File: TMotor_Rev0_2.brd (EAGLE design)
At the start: 91.5 x 74.3 mm, 78 parts, among them J1 5015680507, J10 5015680207, J2 5015680507, J7 5015680207, J8 5015680207, J9 5015680207, U1 INA125U, U2 INA125U, U3 INA125U, U4 INA125U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

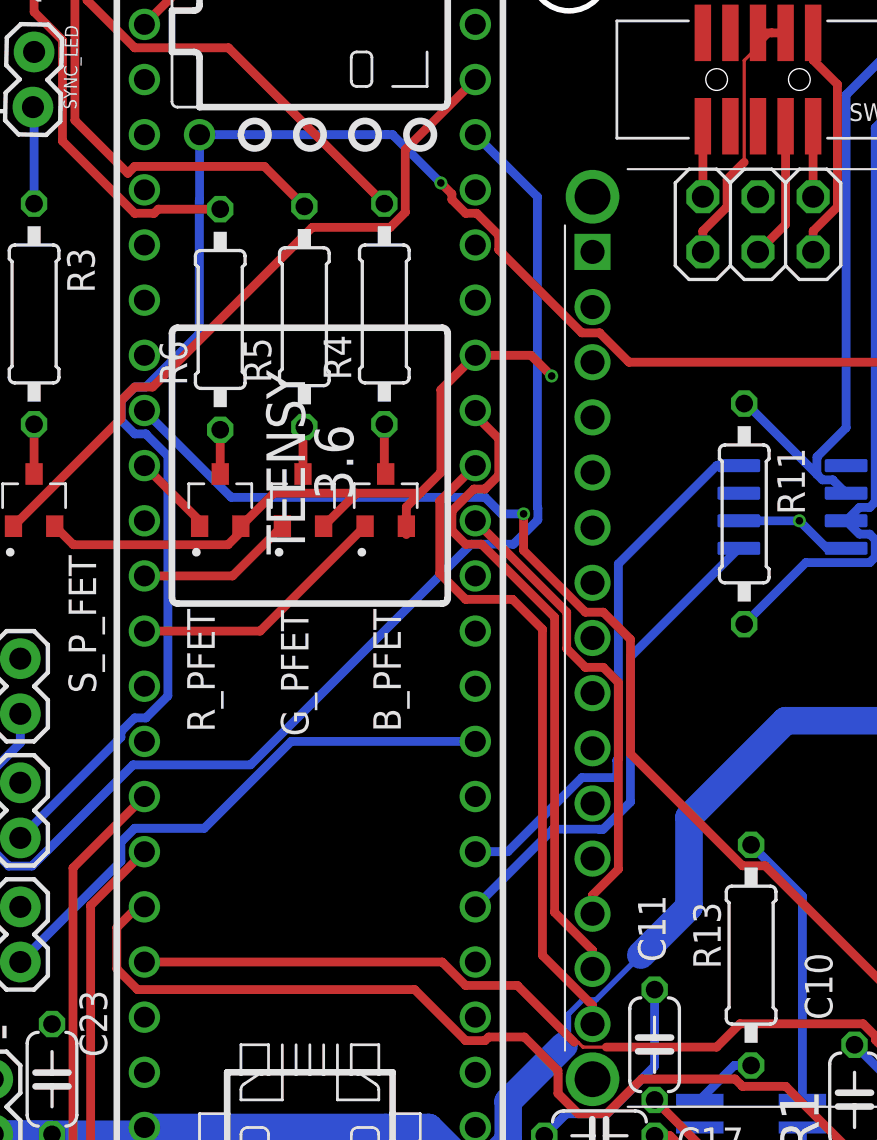
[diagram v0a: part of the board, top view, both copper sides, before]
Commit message: created CIPO COPI transfer spot
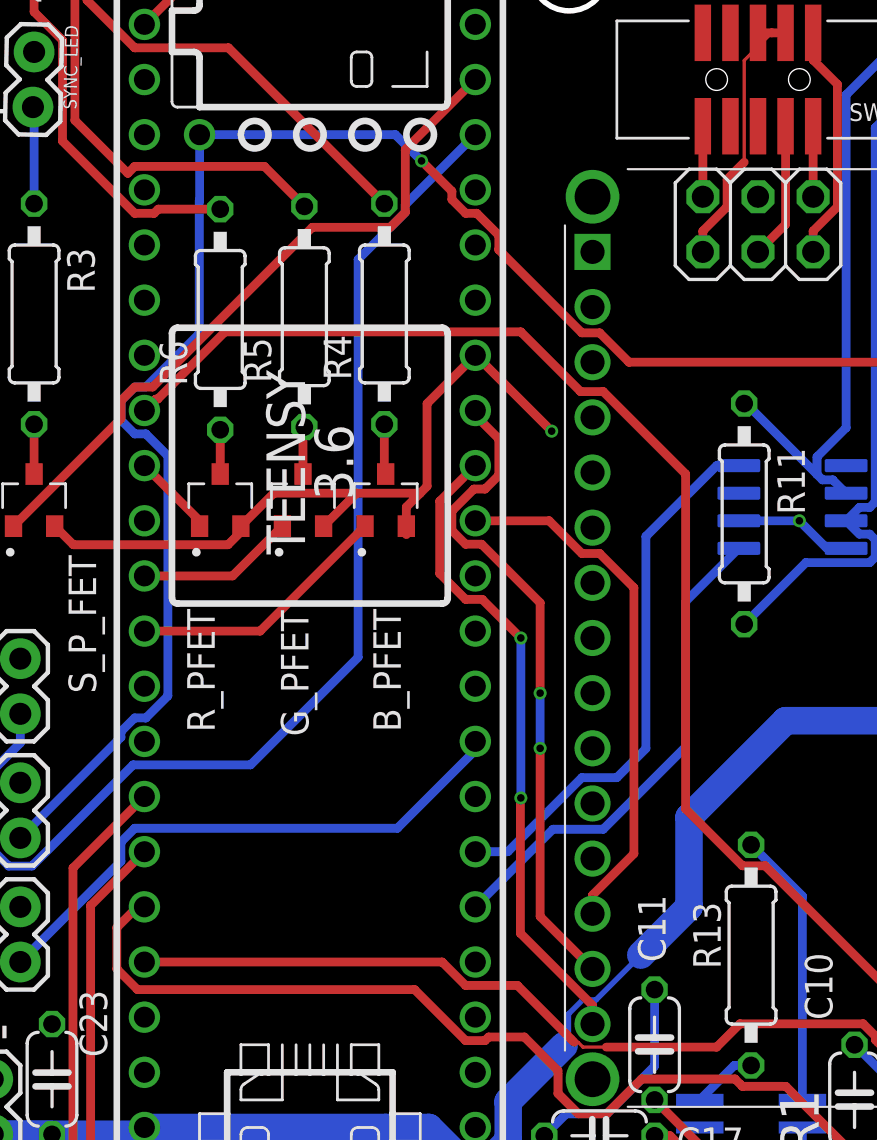
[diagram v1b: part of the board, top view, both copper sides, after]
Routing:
- net SCK: track 51.7 -> 59.6 mm, vias 1 -> 0
- net SYNC_DEFAULT: track 57.8 -> 54.2 mm
- net NANO_CS: track 21.8 -> 24.4 mm
- net 3.3V: track 62.1 -> 63.1 mm
- net MISO: track 30.6 -> 29.8 mm, vias 0 -> 2
- net MOSI: vias 0 -> 2

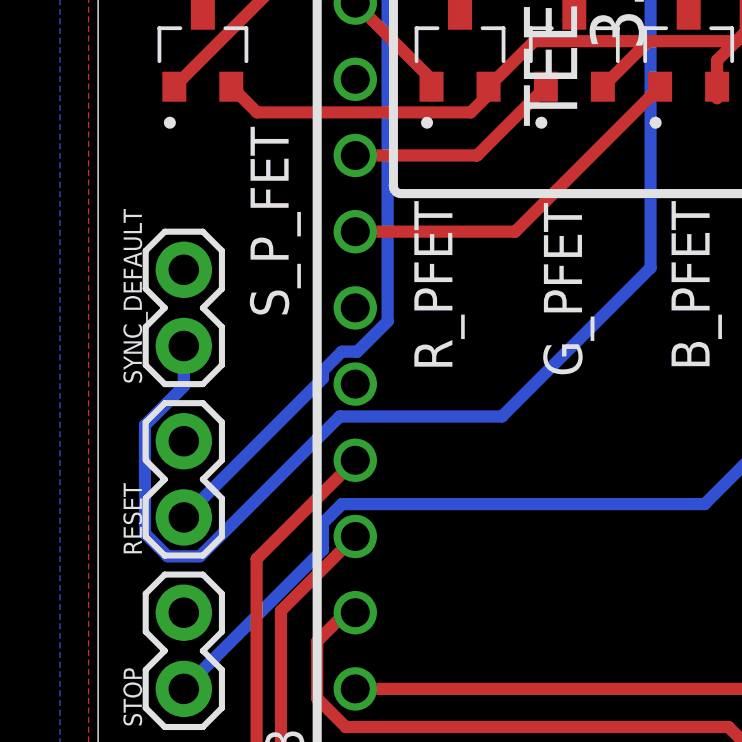
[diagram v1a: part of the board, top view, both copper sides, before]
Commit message: repositioned headers for switches
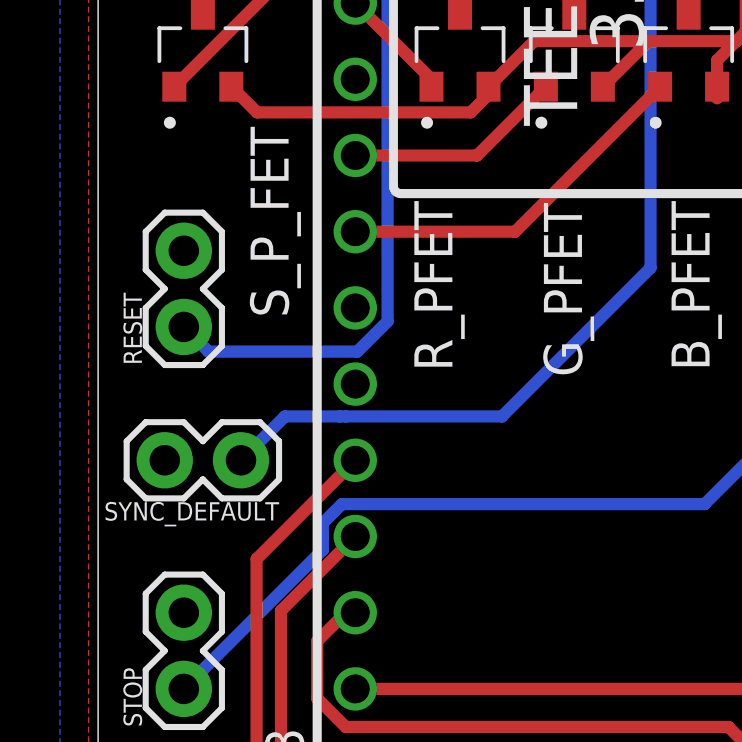
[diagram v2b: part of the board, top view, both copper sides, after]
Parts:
- moved RESET 6.35 mm to (-30.8, 35.9)
- moved SYNC_DEFAULT 4.26 mm to (-28.9, 31.4), turned to 180 degrees
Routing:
- net SYNC_DEFAULT: track 54.2 -> 42.6 mm
- net RESET: track 76.8 -> 74.7 mm
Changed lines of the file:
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@@
 </element>
 <element name="U$1" library="Teensy356" package="TEENSY_3.5/3.6_EXTERNAL_W/RESET" value="TEENSY_3.5/3.6_EXTERNAL_W/RESET" x="-17.4625" y="44.1325" smashed="yes" rot="R90"/>
-<element name="RESET" library="SparkFun-Connectors" library_urn="urn:adsk.eagle:library:513" package="1X02" package3d_urn="urn:adsk.eagle:package:38039/1" value="" x="-30.7975" y="29.5275" smashed="yes" rot="R90">
-<attribute name="NAME" x="-32.1945" y="28.2575" size="0.6096" layer="25" font="vector" ratio="20" rot="R90"/>
-<attribute name="VALUE" x="-28.7655" y="28.2575" size="0.6096" layer="27" font="vector" ratio="20" rot="R90"/>
-</element>
-<element name="SYNC_DEFAULT" library="SparkFun-Connectors" library_urn="urn:adsk.eagle:library:513" package="1X02" package3d_urn="urn:adsk.eagle:package:38039/1" value="" x="-30.7975" y="35.2425" smashed="yes" rot="R90">
-<attribute name="NAME" x="-32.1945" y="33.9725" size="0.6096" layer="25" font="vector" ratio="20" rot="R90"/>
-<attribute name="VALUE" x="-28.7655" y="33.9725" size="0.6096" layer="27" font="vector" ratio="20" rot="R90"/>
+<element name="RESET" library="SparkFun-Connectors" library_urn="urn:adsk.eagle:library:513" package="1X02" package3d_urn="urn:adsk.eagle:package:38039/1" value="" x="-30.7975" y="35.8775" smashed="yes" rot="R90">
+<attribute name="NAME" x="-32.1945" y="34.6075" size="0.6096" layer="25" font="vector" ratio="20" rot="R90"/>
+<attribute name="VALUE" x="-28.7655" y="34.6075" size="0.6096" layer="27" font="vector" ratio="20" rot="R90"/>
+</element>
+<element name="SYNC_DEFAULT" library="SparkFun-Connectors" library_urn="urn:adsk.eagle:library:513" package="1X02" package3d_urn="urn:adsk.eagle:package:38039/1" value="" x="-28.8925" y="31.4325" smashed="yes" rot="R180">
+<attribute name="NAME" x="-27.6225" y="30.0355" size="0.6096" layer="25" font="vector" ratio="20" rot="R180"/>
+<attribute name="VALUE" x="-27.6225" y="33.4645" size="0.6096" layer="27" font="vector" ratio="20" rot="R180"/>
 </element>
 <element name="U$4" library="XT30PW-M" package="XT30PWF" value="XT30PW-F" x="50.8" y="78.74" smashed="yes">
@@
 <signal name="SYNC_DEFAULT">
 <contactref element="SYNC_DEFAULT" pad="1"/>
-<wire x1="-32.0929" y1="28.990925" x2="-31.334075" y2="28.2321" width="0.4064" layer="16"/>
-<wire x1="-31.334075" y1="28.2321" x2="-30.260925" y2="28.2321" width="0.4064" layer="16"/>
-<wire x1="-32.0929" y1="32.604075" x2="-32.0929" y2="28.990925" width="0.4064" layer="16"/>
-<wire x1="-30.260925" y1="28.2321" x2="-25.600025" y2="32.893" width="0.4064" layer="16"/>
-<wire x1="-25.600025" y1="32.893" x2="-20.193" y2="32.893" width="0.4064" layer="16"/>
-<wire x1="-30.7975" y1="35.2425" x2="-30.7975" y2="33.899475" width="0.4064" layer="16"/>
-<wire x1="-30.7975" y1="33.899475" x2="-32.0929" y2="32.604075" width="0.4064" layer="16"/>
+<wire x1="-25.600025" y1="32.893" x2="-25.4" y2="32.893" width="0.4064" layer="16"/>
 <contactref element="U$1" pad="27"/>
+<wire x1="-25.4" y1="32.893" x2="-20.193" y2="32.893" width="0.4064" layer="16"/>
 <wire x1="-20.193" y1="32.893" x2="-15.24" y2="37.846" width="0.4064" layer="16"/>
 <wire x1="-13.0683" y1="58.3377" x2="-13.0683" y2="58.6867" width="0.4064" layer="16"/>
@@
 <wire x1="-15.24" y1="56.166" x2="-13.0683" y2="58.3377" width="0.4064" layer="16"/>
 <wire x1="-15.24" y1="37.846" x2="-15.24" y2="56.166" width="0.4064" layer="16"/>
+<wire x1="-25.600025" y1="32.893" x2="-27.432" y2="32.893" width="0.4064" layer="16"/>
+<wire x1="-27.432" y1="32.893" x2="-28.8925" y2="31.4325" width="0.4064" layer="16"/>
 </signal>
 <signal name="N$17">
@@
 <wire x1="-26.162" y1="49.65964375" x2="-26.162" y2="48.76535625" width="0.4064" layer="16"/>
 <wire x1="-26.162" y1="48.76535625" x2="-25.52964375" y2="48.133" width="0.4064" layer="16"/>
-<wire x1="-25.52964375" y1="35.052" x2="-26.162" y2="34.41964375" width="0.4064" layer="16"/>
-<wire x1="-26.162" y1="34.41964375" x2="-26.162" y2="34.163" width="0.4064" layer="16"/>
-<wire x1="-26.162" y1="34.163" x2="-30.7975" y2="29.5275" width="0.4064" layer="16"/>
+<wire x1="-30.7975" y1="35.8775" x2="-29.972" y2="35.052" width="0.4064" layer="16"/>
+<wire x1="-25.01635625" y1="35.052" x2="-29.972" y2="35.052" width="0.4064" layer="16"/>
 <wire x1="-22.5552" y1="52.75315625" x2="-25.01635625" y2="50.292" width="0.4064" layer="16"/>
 <wire x1="-25.01635625" y1="50.292" x2="-25.52964375" y2="50.292" width="0.4064" layer="16"/>
@@
 <wire x1="-24.003" y1="47.11964375" x2="-24.003" y2="36.06535625" width="0.4064" layer="16"/>
 <wire x1="-24.003" y1="36.06535625" x2="-25.01635625" y2="35.052" width="0.4064" layer="16"/>
-<wire x1="-25.01635625" y1="35.052" x2="-25.52964375" y2="35.052" width="0.4064" layer="16"/>
 <wire x1="-10.28964375" y1="58.293" x2="-10.922" y2="58.92535625" width="0.4064" layer="1"/>
 <wire x1="-10.922" y1="58.92535625" x2="-10.922" y2="59.309" width="0.4064" layer="1"/>

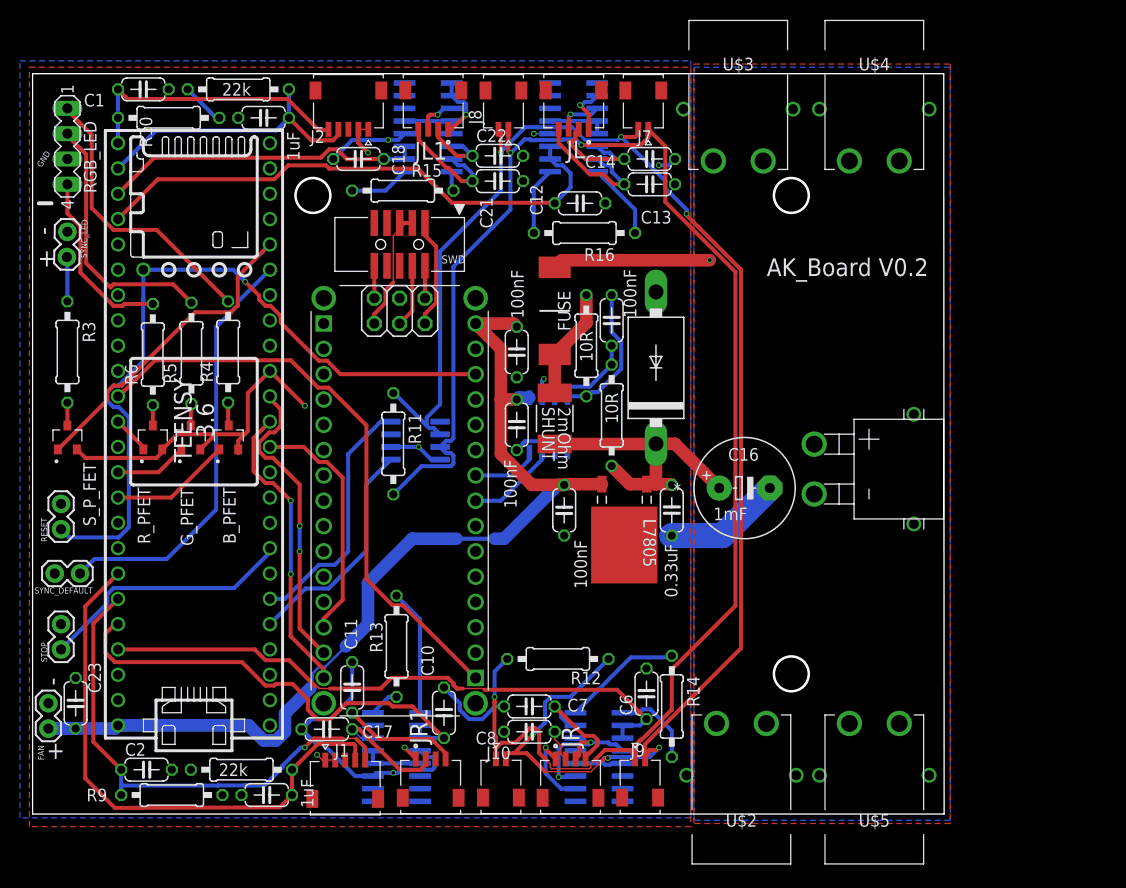
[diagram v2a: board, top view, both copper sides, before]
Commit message: added fuses and fets for motor power
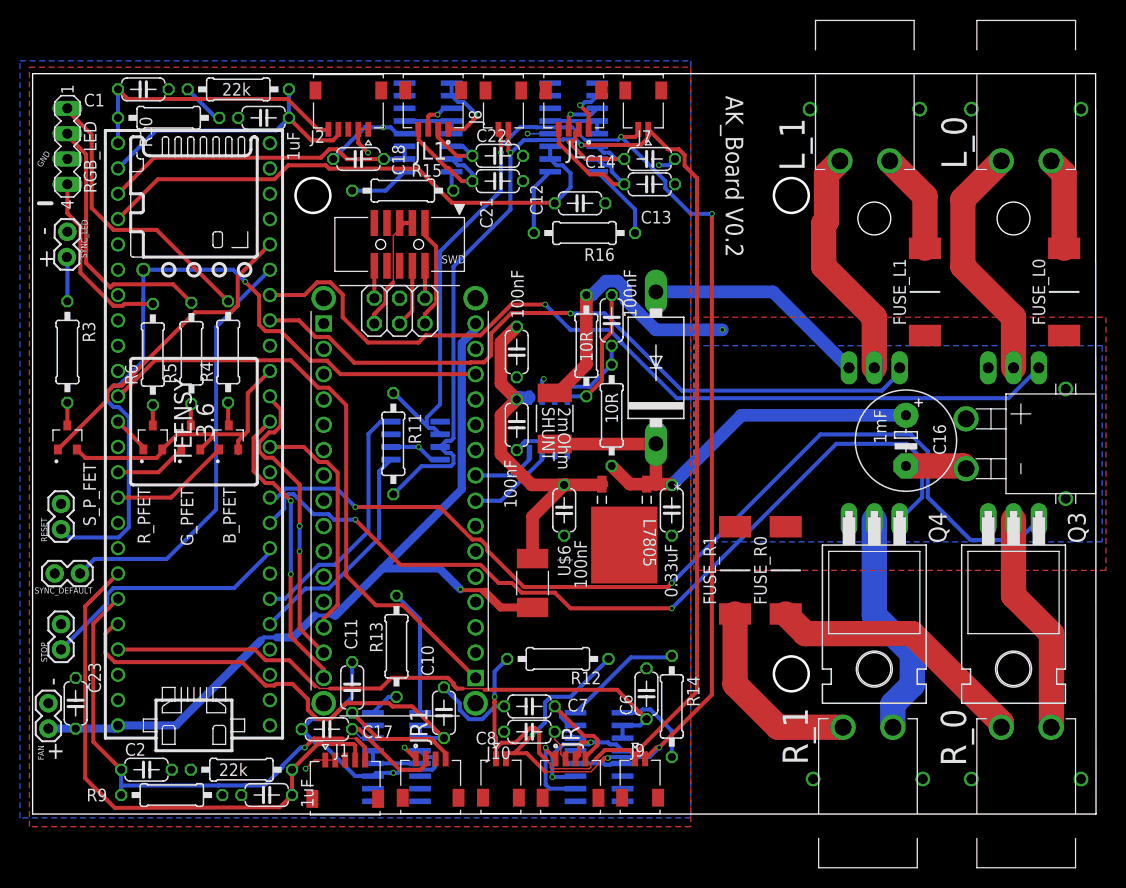
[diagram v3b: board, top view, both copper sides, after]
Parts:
- removed FUSE: 0456020.ER, SamacSys_Parts:FUSC10131X312N
- removed U$2, U$3, U$4, U$5: XT30PW-F, XT30PW-M:XT30PWF
- added FUSE_L0, FUSE_L1, FUSE_R0, FUSE_R1: 0456020.ER, SamacSys_Parts:FUSC10131X312N
- added L_0, L_1, R_0, R_1: XT30PW-F, XT30PW-M:XT30PWF
- added Q1, Q2, Q3, Q4: IRLB8721PBFTO220H, IRLB8721PBF:TO220H
- added U$6: 0458002.DR, SnapEDA-Library (1):FUSE_LITTEL_448
- moved C16 16.9 mm to (54.0, 44.8), turned to 270 degrees
- moved U$9 15.5 mm to (60.0, 44.5)
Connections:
- removed net PF_VCC: FUSE.1, R2.2, SHUNT.2
- new net L_0_ENABLE: Q1.1, U$1.26
- new net L_1_ENABLE: Q2.1, U$1.25
- new net N$43: FUSE_L0.2, L_0.+
- new net N$46: FUSE_L1.2, L_1.+
- new net N$47: FUSE_R1.2, R_1.+
- new net N$48: FUSE_R0.2, R_0.+
- new net N$49: L_0.-, Q1.2
- new net N$50: Q3.2, R_0.-
- new net N$51: Q4.2, R_1.-
- new net N$52: L_1.-, Q2.2
- new net R_0_ENABLE: Q3.1, U$1.8
- new net R_1_ENABLE: Q4.1, U$1.7
- new net VIN_PF: C23.2, FAN.1, U$1.VIN, U$6.2, USB.A15
- net GND: now also Q1.3, Q2.3, Q3.3, Q4.3; no longer U$2.-, U$3.-, U$4.-, U$5.-
- net VCC: now also FUSE_L0.1, FUSE_L1.1, FUSE_R0.1, FUSE_R1.1, R2.2, SHUNT.2; no longer FUSE.2, U$2.+, U$3.+, U$4.+, U$5.+
- net VIN: now also U$6.1; no longer C23.2, FAN.1, U$1.VIN, USB.A15
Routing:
- net R_0_ENABLE: track 0.00 -> 96.1 mm, vias 0 -> 2
- net L_0_ENABLE: track 0.00 -> 88.3 mm, vias 0 -> 1
- net R_1_ENABLE: track 0.00 -> 86.5 mm, vias 0 -> 2
- net VIN_PF: track 0.00 -> 85.4 mm, vias 0 -> 1
- net L_1_ENABLE: track 0.00 -> 72.8 mm, vias 0 -> 1
- net VIN: track 102.9 -> 37.0 mm
- net N$48: track 0.00 -> 26.6 mm
- net N$49: track 0.00 -> 24.5 mm
- net N$52: track 0.00 -> 23.5 mm
- net N$51: track 0.00 -> 23.2 mm
- net N$50: track 0.00 -> 22.4 mm
- net N$47: track 0.00 -> 19.7 mm
- net GND: track 101.3 -> 120.2 mm
- net L7_VIN: track 29.2 -> 47.4 mm
- net VCC: track 15.8 -> 27.9 mm
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- added copper zone on layer 16, net GND
- added copper zone on layer 1, net VCC
- removed copper zone on layer 16, net VCC
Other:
- board size 91.5 x 74.3 mm -> 106.7 x 74.3 mm
- board text added: "1."
- board text added: "2."
- board text added: "3."
- board text added: "4."
- board text added: "Updates to make:"

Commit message: added motor fets to top level
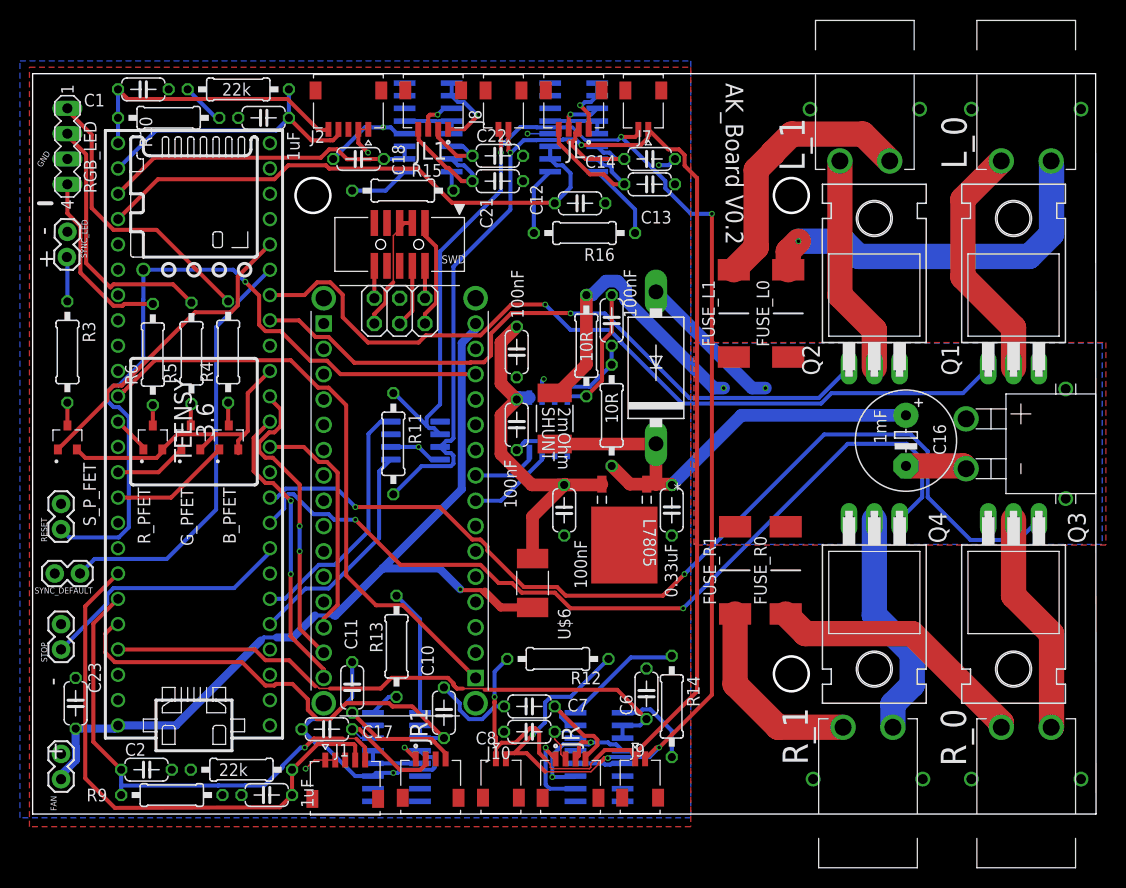
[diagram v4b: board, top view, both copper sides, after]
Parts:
- moved FUSE_L0 27.8 mm to (42.2, 57.5)
- moved FUSE_L1 19.3 mm to (36.7, 57.5)
- moved FAN 5.24 mm to (-30.8, 10.8)
- flipped Q1 to the top
- flipped Q2 to the top
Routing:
- net N$43: track 9.31 -> 37.2 mm, vias 0 -> 1
- net N$46: track 10.2 -> 27.0 mm
- net GND: track 120.2 -> 112.6 mm, vias 10 -> 11
- net L_1_ENABLE: track 72.8 -> 68.0 mm
- net L_0_ENABLE: track 88.3 -> 83.7 mm
- net VIN_PF: track 85.4 -> 88.4 mm
- net VCC: track 27.9 -> 30.4 mm
- net N$52: track 23.5 -> 22.2 mm
- net R_0_ENABLE: track 96.1 -> 96.8 mm
